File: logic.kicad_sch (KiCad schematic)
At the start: 77 parts, among them J10 I2C, J4 SMBUS, J5 HanRun_HR911105A, Q24 2N7002, Q25 AO3401A, SW2 SW_Push, U10 LAN8720A, U11 74HC595, U17 N066-6448TSWEG03-H28, U8 SY8120B1ABC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

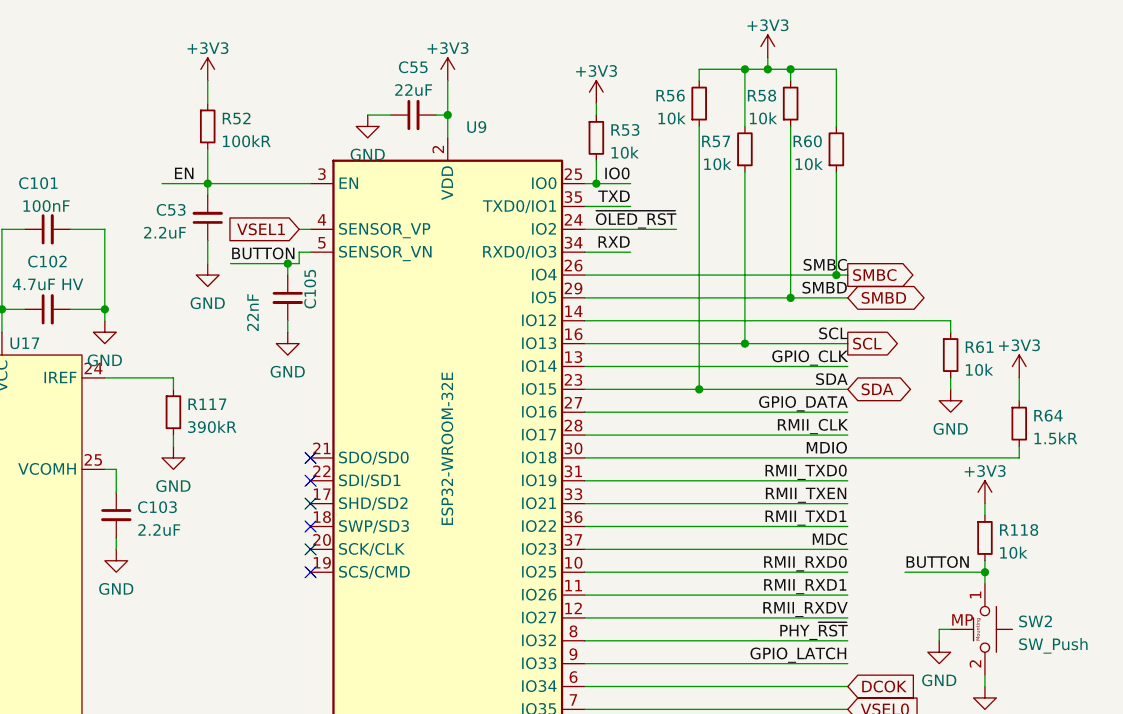
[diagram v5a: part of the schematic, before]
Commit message: Swap GPIO2 and GPIO23 to ensure UART download mode can be entered
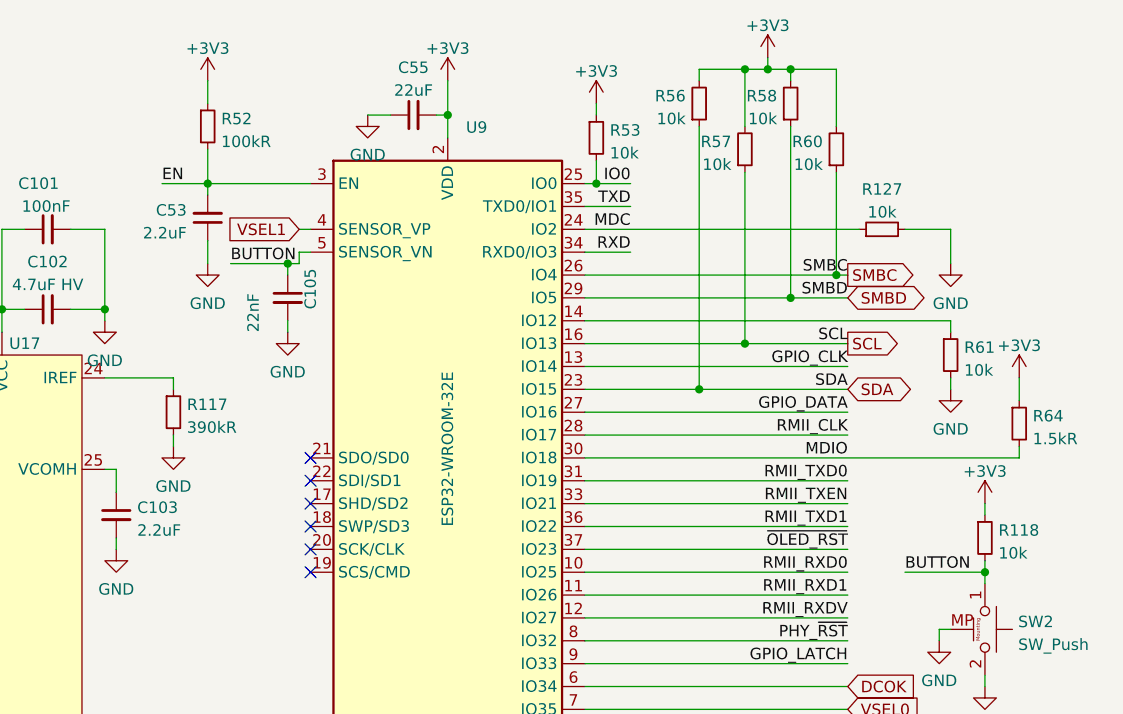
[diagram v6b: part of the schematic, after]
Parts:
- added R127: 10k, Resistor_SMD:R_0402_1005Metric, symbol Device:R_Small
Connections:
- net GND: now also R127.2
- net MDC: now also U9.24 (IO2), R127.1; no longer U9.37 (IO23)
- net ~{OLED_RST}: now also U9.37 (IO23); no longer U9.24 (IO2)
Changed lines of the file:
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@@
     (stroke (width 0) (type default) (color 0 0 0 0))
   )
-  (wire (pts (xy 227.33 40.64) (xy 237.49 40.64))
+  (wire (pts (xy 227.33 40.64) (xy 257.81 40.64))
     (stroke (width 0) (type default) (color 0 0 0 0))
   )
@@
     (stroke (width 0) (type default) (color 0 0 0 0))
   )
+  (wire (pts (xy 267.97 40.64) (xy 262.89 40.64))
+    (stroke (width 0) (type default) (color 0 0 0 0))
+  )
   (wire (pts (xy 74.93 74.93) (xy 80.01 74.93))
     (stroke (width 0) (type default) (color 0 0 0 0))
@@
     (stroke (width 0) (type default) (color 0 0 0 0))
   )
+  (wire (pts (xy 267.97 44.45) (xy 267.97 40.64))
+    (stroke (width 0) (type default) (color 0 0 0 0))
+  )
   (wire (pts (xy 194.31 50.8) (xy 194.31 52.07))
     (stroke (width 0) (type default) (color 0 0 0 0))
@@
     (effects (font (size 1.27 1.27)) (justify right bottom))
   )
-  (label "EN" (at 181.61 35.56 0)
+  (label "EN" (at 180.34 35.56 0)
     (effects (font (size 1.27 1.27)) (justify left bottom))
   )
@@
     (effects (font (size 1.27 1.27)) (justify left bottom))
   )
-  (label "~{OLED_RST}" (at 237.49 40.64 180)
+  (label "~{OLED_RST}" (at 256.54 76.2 180)
     (effects (font (size 1.27 1.27)) (justify right bottom))
   )
@@
     (effects (font (size 1.27 1.27)) (justify right bottom))
   )
-  (label "MDC" (at 256.54 76.2 180)
+  (label "MDC" (at 232.41 40.64 180)
     (effects (font (size 1.27 1.27)) (justify right bottom))
   )
@@
     (pin "2")
   )
+  (symbol (lib_id "power:GND") (at 267.97 44.45 0) (unit 1)
+    (in_bom yes) (on_board yes) (fields_autoplaced)
+    (property "Reference" "#PWR0315" (id 0) (at 267.97 50.8 0)
+      (effects (font (size 1.27 1.27)) hide)
+    )
+    (property "Value" "GND" (id 1) (at 267.97 48.8934 0))
+    (property "Footprint" "" (id 2) (at 267.97 44.45 0)
+      (effects (font (size 1.27 1.27)) hide)
+    )
+    (property "Datasheet" "" (id 3) (at 267.97 44.45 0)
+      (effects (font (size 1.27 1.27)) hide)
+    )
+    (pin "1")
+  )
   (symbol (lib_id "power:GND") (at 181.61 64.77 0) (unit 1)
     (in_bom yes) (on_board yes) (fields_autoplaced)
@@
       (effects (font (size 1.27 1.27)) hide)
     )
+    (pin "1")
+    (pin "2")
+  )
+  (symbol (lib_id "Device:R_Small") (at 260.35 40.64 90) (unit 1)
+    (in_bom yes) (on_board yes) (fields_autoplaced)
+    (property "Reference" "R127" (id 0) (at 260.35 36.2036 90))
+    (property "Value" "10k" (id 1) (at 260.35 38.7405 90))
+    (property "Footprint" "Resistor_SMD:R_0402_1005Metric" (id 2) (at 260.35 40.64 0)
+      (effects (font (size 1.27 1.27)) hide)
+    )
+    (property "Datasheet" "~" (id 3) (at 260.35 40.64 0)
+      (effects (font (size 1.27 1.27)) hide)
+    )
+    (property "LCSC" "C25744" (id 4) (at 260.35 40.64 0)
+      (effects (font (size 1.27 1.27)) hide)
+    )

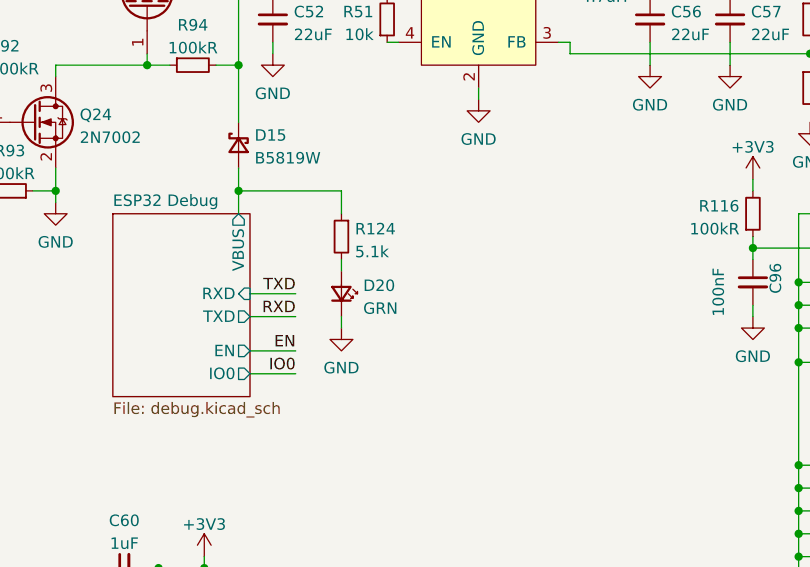
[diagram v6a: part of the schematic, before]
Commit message: Compensate leakage through VBUS schottky diode
Add 10k resistor from VBUS to GND to compensate for schottky diode
leakage.
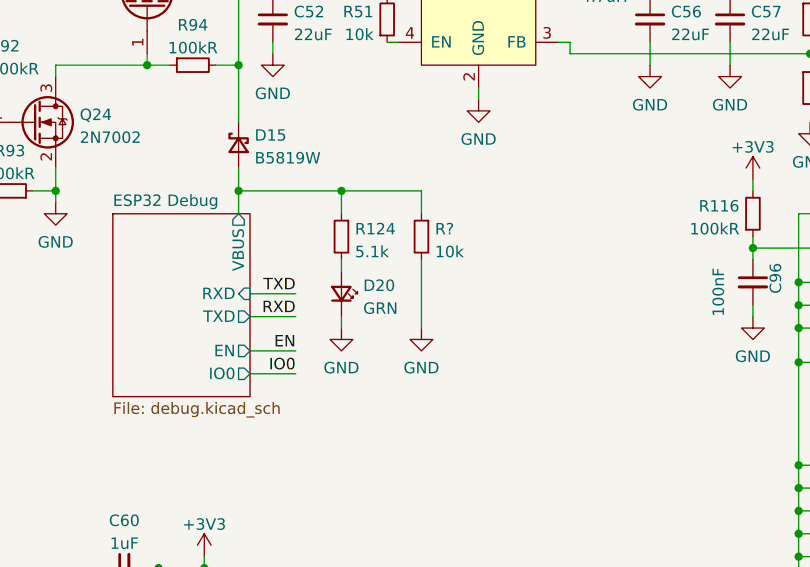
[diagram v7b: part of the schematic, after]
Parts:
- added R?: 10k, Resistor_SMD:R_0402_1005Metric, symbol Device:R_Small
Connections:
- net ESP32 Debug/VBUS: now also R?.1
- net GND: now also R?.2
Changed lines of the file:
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@@
   (junction (at 228.6 140.97) (diameter 0) (color 0 0 0 0)
+  )
+  (junction (at 85.09 57.15) (diameter 0) (color 0 0 0 0)
   )
   (junction (at 120.65 124.46) (diameter 0) (color 0 0 0 0)
@@
     (stroke (width 0) (type default) (color 0 0 0 0))
   )
+  (wire (pts (xy 93.98 64.77) (xy 93.98 72.39))
+    (stroke (width 0) (type default) (color 0 0 0 0))
+  )
   (wire (pts (xy 24.13 135.89) (xy 49.53 135.89))
     (stroke (width 0) (type default) (color 0 0 0 0))
@@
     (stroke (width 0) (type default) (color 0 0 0 0))
   )
+  (wire (pts (xy 85.09 57.15) (xy 93.98 57.15))
+    (stroke (width 0) (type default) (color 0 0 0 0))
+  )
   (wire (pts (xy 44.45 34.29) (xy 58.42 34.29))
     (stroke (width 0) (type default) (color 0 0 0 0))
@@
   )
   (wire (pts (xy 227.33 48.26) (xy 250.19 48.26))
+    (stroke (width 0) (type default) (color 0 0 0 0))
+  )
+  (wire (pts (xy 93.98 57.15) (xy 93.98 59.69))
     (stroke (width 0) (type default) (color 0 0 0 0))
   )
@@
     (pin "1")
   )
+  (symbol (lib_id "Device:R_Small") (at 93.98 62.23 0) (mirror y) (unit 1)
+    (in_bom yes) (on_board yes) (fields_autoplaced)
+    (property "Reference" "R?" (id 0) (at 95.4786 61.3953 0)
+      (effects (font (size 1.27 1.27)) (justify right))
+    )
+    (property "Value" "10k" (id 1) (at 95.4786 63.9322 0)
+      (effects (font (size 1.27 1.27)) (justify right))
+    )
+    (property "Footprint" "Resistor_SMD:R_0402_1005Metric" (id 2) (at 93.98 62.23 0)
+      (effects (font (size 1.27 1.27)) hide)
+    )
+    (property "Datasheet" "~" (id 3) (at 93.98 62.23 0)
+      (effects (font (size 1.27 1.27)) hide)
+    )
+    (property "LCSC" "C25744" (id 4) (at 93.98 62.23 0)
+      (effects (font (size 1.27 1.27)) hide)
+    )
+    (pin "1")
+    (pin "2")
+  )
   (symbol (lib_id "Device:C_Small") (at 76.2 107.95 90) (unit 1)
     (in_bom yes) (on_board yes) (fields_autoplaced)
@@
     (pin "2")
   )
+  (symbol (lib_id "power:GND") (at 93.98 72.39 0) (unit 1)
+    (in_bom yes) (on_board yes) (fields_autoplaced)
+    (property "Reference" "#PWR?" (id 0) (at 93.98 78.74 0)
+      (effects (font (size 1.27 1.27)) hide)
+    )
+    (property "Value" "GND" (id 1) (at 93.98 76.8334 0))
+    (property "Footprint" "" (id 2) (at 93.98 72.39 0)
+      (effects (font (size 1.27 1.27)) hide)
+    )
+    (property "Datasheet" "" (id 3) (at 93.98 72.39 0)
+      (effects (font (size 1.27 1.27)) hide)
+    )
+    (pin "1")
+  )
   (symbol (lib_id "Device:R_Small") (at 240.03 26.67 0) (mirror x) (unit 1)

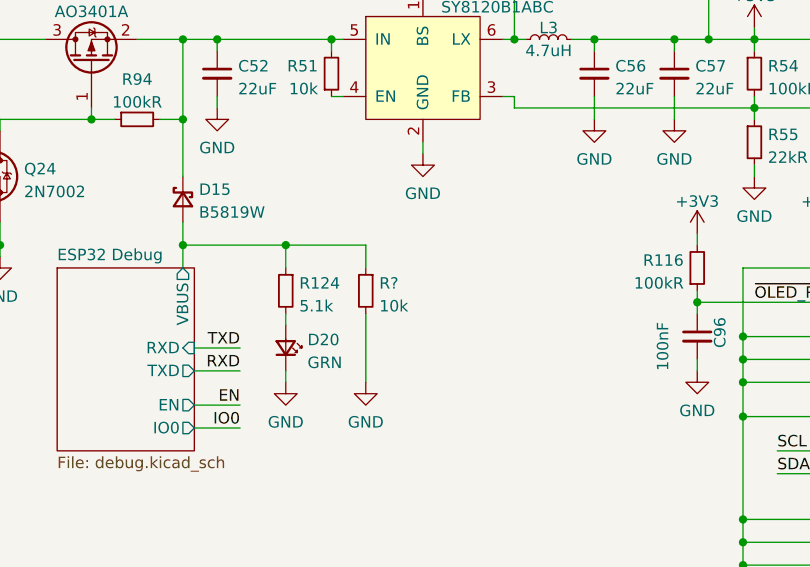
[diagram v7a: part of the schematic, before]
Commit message: Add missing annotations
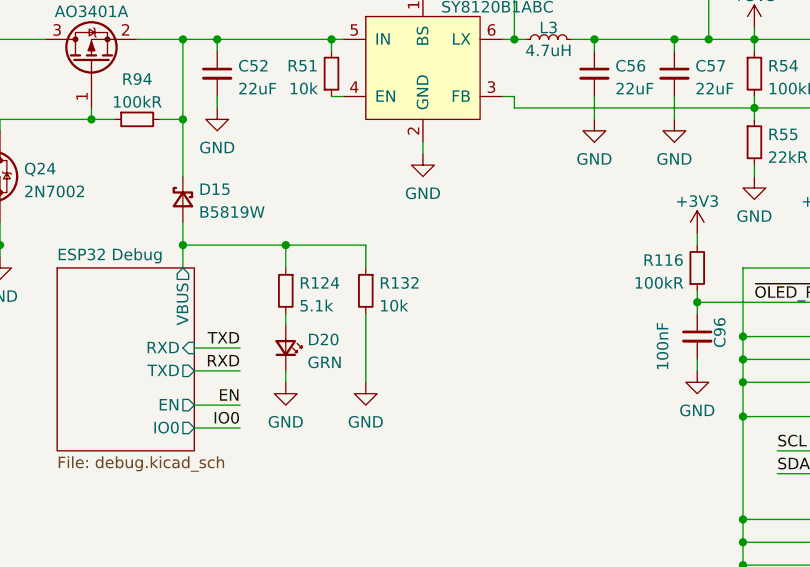
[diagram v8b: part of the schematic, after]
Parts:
- gave numbers to parts that had none: 1
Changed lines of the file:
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@@
   (symbol (lib_id "Device:R_Small") (at 93.98 62.23 0) (mirror y) (unit 1)
     (in_bom yes) (on_board yes) (fields_autoplaced)
-    (property "Reference" "R?" (id 0) (at 95.4786 61.3953 0)
+    (property "Reference" "R132" (id 0) (at 95.4786 61.3953 0)
       (effects (font (size 1.27 1.27)) (justify right))
     )
@@
   (symbol (lib_id "power:GND") (at 93.98 72.39 0) (unit 1)
     (in_bom yes) (on_board yes) (fields_autoplaced)
-    (property "Reference" "#PWR?" (id 0) (at 93.98 78.74 0)
+    (property "Reference" "#PWR0317" (id 0) (at 93.98 78.74 0)
       (effects (font (size 1.27 1.27)) hide)
     )
